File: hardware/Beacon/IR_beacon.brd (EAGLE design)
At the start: 25.6 x 25.6 mm, 11 parts

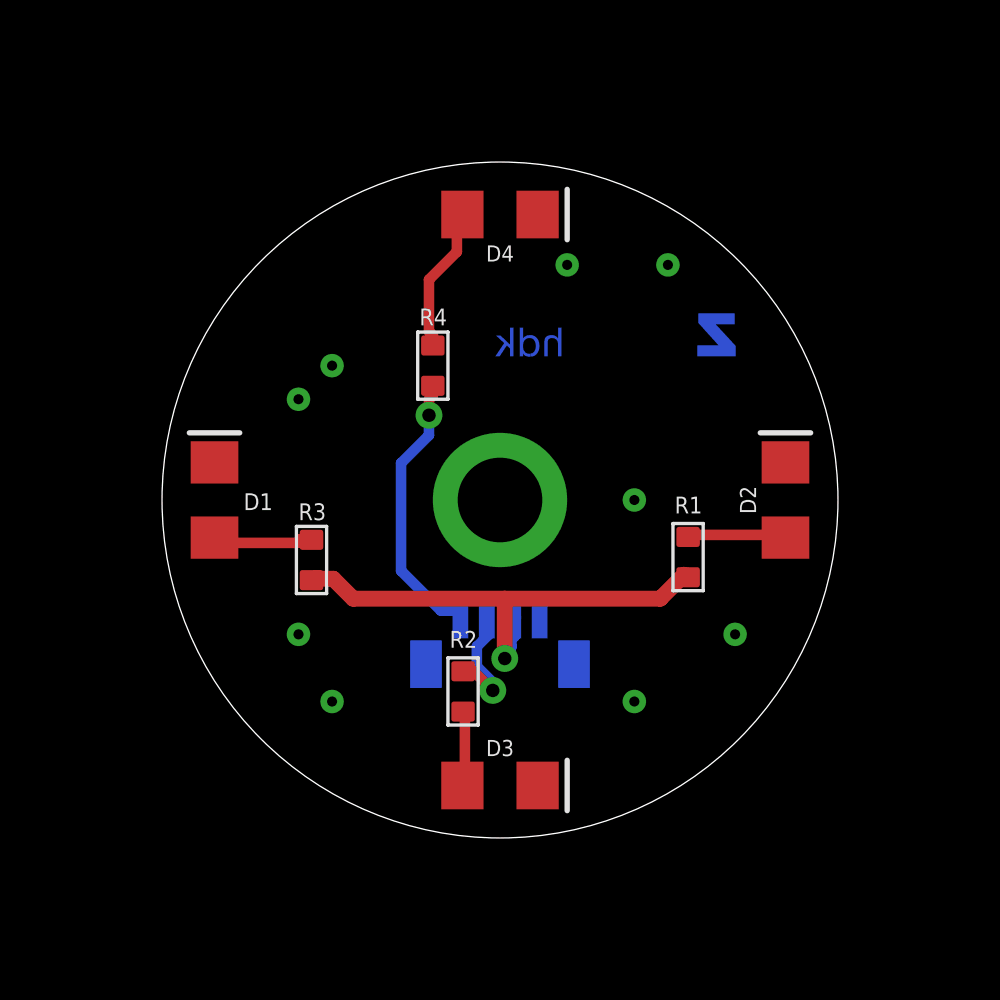
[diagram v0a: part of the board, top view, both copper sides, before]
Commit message: Finished Cad files for beacon, and added new 5 bit patern for markers.
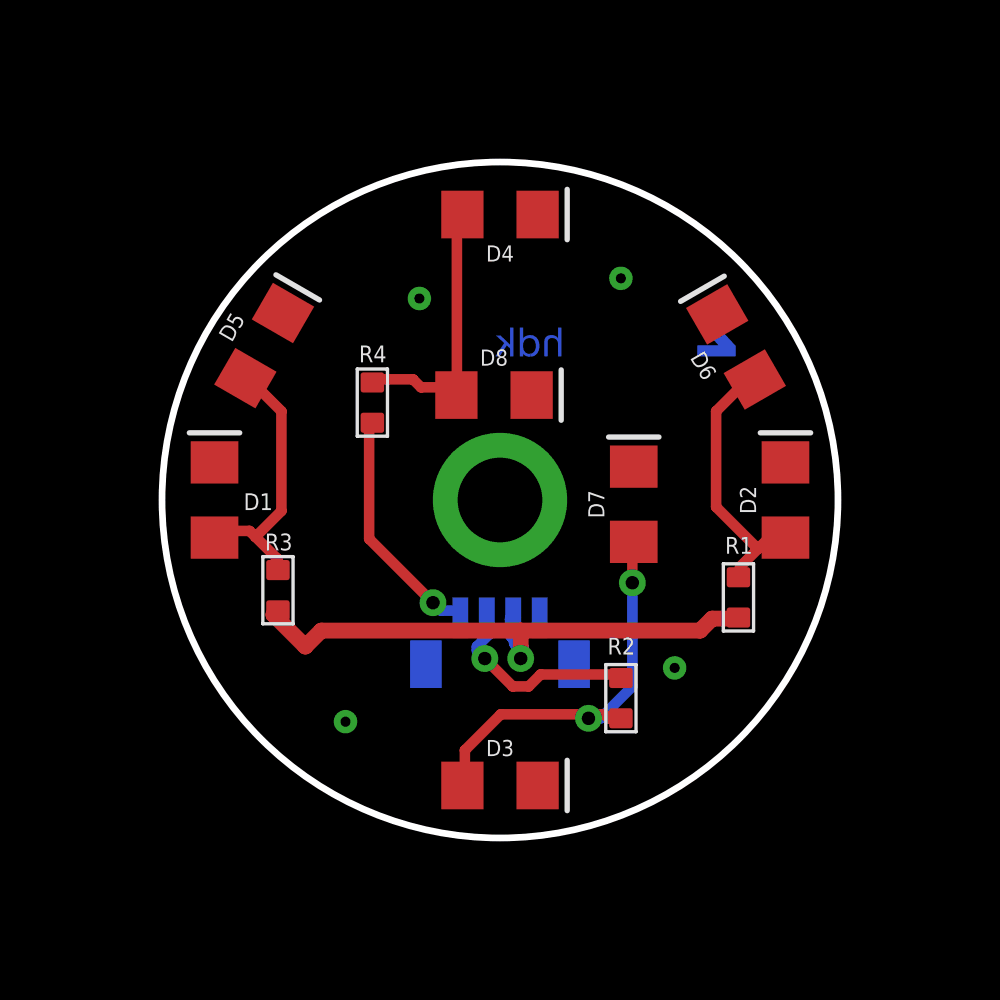
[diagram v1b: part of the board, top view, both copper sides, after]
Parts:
- added D5, D6, D7, D8: (no value), SparkFun-LED:FKIT-LED-1206
- moved R2 5.97 mm to (40.1, 12.8)
- moved R4 2.68 mm to (30.7, 24.0)
- moved R1 2.44 mm to (44.6, 16.6)
- moved R3 1.71 mm to (27.2, 16.9)
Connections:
- net GND: now also D5.C, D6.C, D7.C, D8.C
- net N$2: now also D5.A
- net N$3: now also D7.A
- net N$4: now also D6.A
- net N$5: now also D8.A
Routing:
- net N$3: track 2.85 -> 15.8 mm, vias 0 -> 2
- net N$2: track 3.81 -> 10.9 mm
- net N$4: track 3.82 -> 10.7 mm
- net N$5: track 5.54 -> 10.9 mm
- net N$6: track 4.68 -> 8.42 mm
- net 3.3V: track 18.9 -> 21.6 mm
- net N$1: track 10.7 -> 9.51 mm
